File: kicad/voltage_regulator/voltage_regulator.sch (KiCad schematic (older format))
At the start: 14 parts

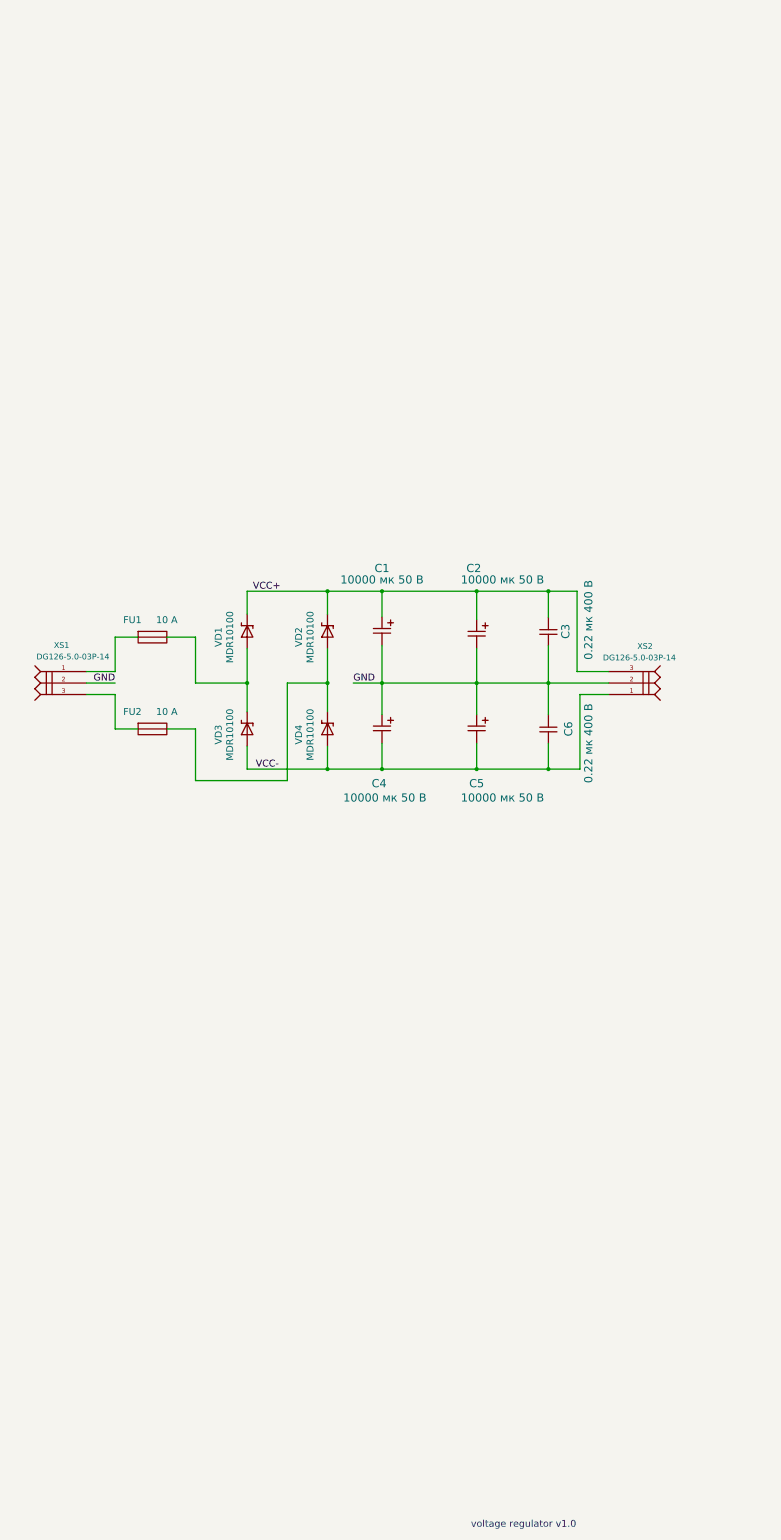
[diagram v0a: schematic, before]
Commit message: Add emc filter.
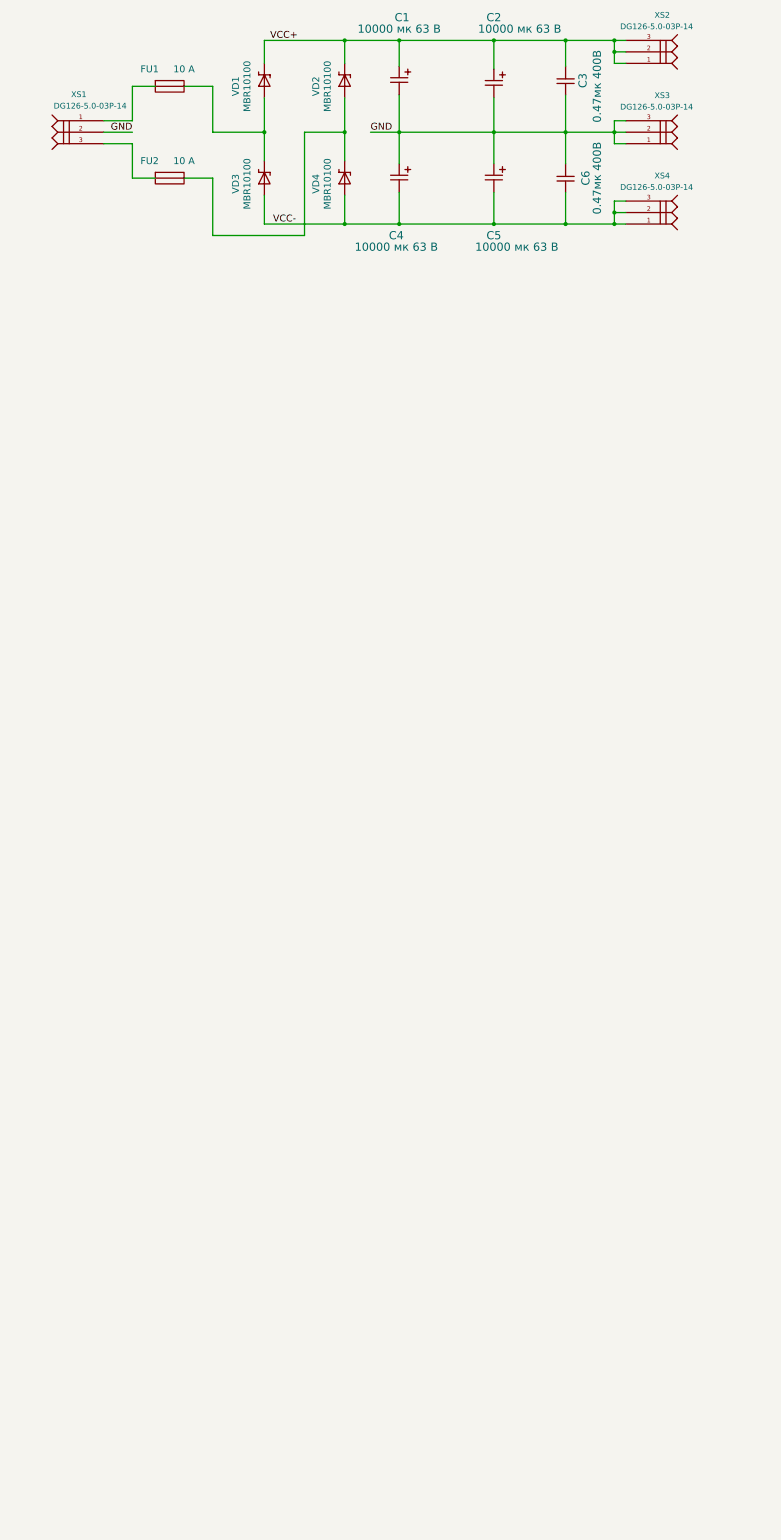
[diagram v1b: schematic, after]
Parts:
- added XS2, XS4: DG126-5.0-03P-14, ~, symbol PIN_F_3
- C1, C2, C4, C5: value 10000 мк 50 В -> 10000 мк 63 В
- C3, C6: value 0.22 мк 400 В -> 0.47мк 400В
- VD1, VD2, VD3, VD4: value MDR10100 -> MBR10100
- renumbered XS2 to XS3
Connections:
- net GND: now also XS3.1, XS3.3
- net VCC+: now also XS2.1, XS2.2, XS2.3; no longer XS3.3
- net VCC-: now also XS4.1, XS4.2, XS4.3; no longer XS3.1
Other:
- note removed: "voltage regulator v1.0"
- moved on the sheet: C1, C2, C3, C4, C5, C6, FU1, FU2, VD1, VD2, VD3, VD4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

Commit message: Moved to kicad 4.0.0
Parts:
- C1, C2, C4, C5: footprint (none) -> LFcomponents:CAPACITOR_CD294
- C3, C6: footprint (none) -> LFcomponents:K73-17
- FU1, FU2: footprint (none) -> LFcomponents:FU_PTF15B
- VD1, VD2, VD3, VD4: footprint (none) -> LFcomponents:TO220_DIOD_VERT_POZ
- XS1, XS2, XS3, XS4: footprint ~ -> DG126-5.0-03P-14~
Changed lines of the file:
@@
 LIBS:LFtransistor
 LIBS:voltage_regulator-cache
-EELAYER 27 0
+EELAYER 25 0
 EELAYER END
 $Descr A4 11693 8268
@@
 F 0 "C5" V 7475 4375 71  0000 C CNN
 F 1 "10000 мк 63 В" V 7575 4575 71  0000 C CNN
-F 2 "" H 6850 4375 60  0001 C CNN
+F 2 "LFcomponents:CAPACITOR_CD294" H 6850 4375 60  0001 C CNN
 F 3 "" H 6850 4375 60  0001 C CNN
 	1    6850 4375
@@
 F 0 "C2" V 6400 3550 71  0000 C CNN
 F 1 "10000 мк 63 В" V 6500 3775 71  0000 C CNN
-F 2 "" H 6850 3550 60  0001 C CNN
+F 2 "LFcomponents:CAPACITOR_CD294" H 6850 3550 60  0001 C CNN
 F 3 "" H 6850 3550 60  0001 C CNN
 	1    6850 3550
@@
 F 0 "C6" H 7600 4450 71  0000 C CNN
 F 1 "0.47мк 400В" H 7600 4350 71  0000 C CNN
-F 2 "" H 7475 4625 60  0001 C CNN
+F 2 "LFcomponents:K73-17" H 7475 4625 60  0001 C CNN
 F 3 "" H 7475 4625 60  0001 C CNN
 	1    7475 4625
@@
 F 0 "C4" V 6650 4350 71  0000 C CNN
 F 1 "10000 мк 63 В" V 6750 4350 71  0000 C CNN
-F 2 "" H 6025 4375 60  0001 C CNN
+F 2 "LFcomponents:CAPACITOR_CD294" H 6025 4375 60  0001 C CNN
 F 3 "" H 6025 4375 60  0001 C CNN
 	1    6025 4375
@@
 F 0 "C1" V 5600 3550 71  0000 C CNN
 F 1 "10000 мк 63 В" V 5700 3525 71  0000 C CNN
-F 2 "" H 6025 3525 60  0001 C CNN
+F 2 "LFcomponents:CAPACITOR_CD294" H 6025 3525 60  0001 C CNN
 F 3 "" H 6025 3525 60  0001 C CNN
 	1    6025 3525
@@
 F 0 "C3" H 7600 3625 71  0000 C CNN
 F 1 "0.47мк 400В" H 7550 3500 71  0000 C CNN
-F 2 "" H 7475 3775 60  0001 C CNN
+F 2 "LFcomponents:K73-17" H 7475 3775 60  0001 C CNN
 F 3 "" H 7475 3775 60  0001 C CNN
 	1    7475 3775
@@
 F 0 "XS3" H 8250 3750 50  0000 L BNN
 F 1 "DG126-5.0-03P-14" H 7950 3850 50  0000 L BNN
-F 2 "~" H 8450 4350 50  0001 C CNN
+F 2 "DG126-5.0-03P-14~" H 8450 4350 50  0001 C CNN
 F 3 "" H 8000 4200 60  0001 C CNN
 	1    8000 4200
@@
 F 0 "FU2" H 3850 4650 60  0000 C CNN
 F 1 "10 A" H 4150 4650 60  0000 C CNN
-F 2 "" H 3900 4500 60  0001 C CNN
+F 2 "LFcomponents:FU_PTF15B" H 3900 4500 60  0001 C CNN
 F 3 "" H 3900 4500 60  0001 C CNN
 	1    3900 4500
@@
 F 0 "VD4" H 5650 4900 60  0000 C CNN
 F 1 "MBR10100" H 5650 4800 60  0000 C CNN
-F 2 "" H 5550 4650 60  0001 C CNN
+F 2 "LFcomponents:TO220_DIOD_VERT_POZ" H 5550 4650 60  0001 C CNN
 F 3 "" H 5550 4650 60  0001 C CNN
 	1    5550 4650
@@
 F 0 "VD3" H 4950 4900 60  0000 C CNN
 F 1 "MBR10100" H 4950 4800 60  0000 C CNN
-F 2 "" H 4850 4650 60  0001 C CNN
+F 2 "LFcomponents:TO220_DIOD_VERT_POZ" H 4850 4650 60  0001 C CNN
 F 3 "" H 4850 4650 60  0001 C CNN
 	1    4850 4650
@@
 F 0 "VD2" H 5650 4050 60  0000 C CNN
 F 1 "MBR10100" H 5650 3950 60  0000 C CNN
-F 2 "" H 5550 3800 60  0001 C CNN
+F 2 "LFcomponents:TO220_DIOD_VERT_POZ" H 5550 3800 60  0001 C CNN
 F 3 "" H 5550 3800 60  0001 C CNN
 	1    5550 3800
@@
 F 0 "FU1" H 3850 3850 60  0000 C CNN
 F 1 "10 A" H 4150 3850 60  0000 C CNN
-F 2 "" H 3900 3700 60  0001 C CNN
+F 2 "LFcomponents:FU_PTF15B" H 3900 3700 60  0001 C CNN
 F 3 "" H 3900 3700 60  0001 C CNN
 	1    3900 3700
@@
 F 0 "XS1" H 3600 4200 50  0000 L BNN
 F 1 "DG126-5.0-03P-14" H 3250 4100 50  0000 L BNN
-F 2 "~" H 3900 4150 50  0001 C CNN
+F 2 "DG126-5.0-03P-14~" H 3900 4150 50  0001 C CNN
 F 3 "" H 3450 4000 60  0001 C CNN
 	1    3450 4000
@@
 F 0 "VD1" H 4950 4050 60  0000 C CNN
 F 1 "MBR10100" H 4950 3950 60  0000 C CNN
-F 2 "" H 4850 3800 60  0001 C CNN
+F 2 "LFcomponents:TO220_DIOD_VERT_POZ" H 4850 3800 60  0001 C CNN
 F 3 "" H 4850 3800 60  0001 C CNN
 	1    4850 3800
@@
 F 0 "XS2" H 8250 3050 50  0000 L BNN
 F 1 "DG126-5.0-03P-14" H 7950 3150 50  0000 L BNN
-F 2 "~" H 8450 3650 50  0001 C CNN
+F 2 "DG126-5.0-03P-14~" H 8450 3650 50  0001 C CNN
 F 3 "" H 8000 3500 60  0001 C CNN
 	1    8000 3500
@@
 F 0 "XS4" H 8250 4450 50  0000 L BNN
 F 1 "DG126-5.0-03P-14" H 7950 4550 50  0000 L BNN
-F 2 "~" H 8450 5050 50  0001 C CNN
+F 2 "DG126-5.0-03P-14~" H 8450 5050 50  0001 C CNN
 F 3 "" H 8000 4900 60  0001 C CNN
 	1    8000 4900

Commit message: Add description to the schemes.
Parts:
- added R1, R2: 20 к, LFcomponents:RESISTOR_1W, symbol RESISTOR_1W
- C1, C2, C4, C5: value 10000 мк 63 В -> 10000 мк 50 В
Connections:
- net GND: now also R1.2, R2.1
- net VCC+: now also R1.1
- net VCC-: now also R2.2
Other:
- moved on the sheet: XS2, XS3, XS4
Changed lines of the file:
@@
 	6850 3300 6850 3550
 Wire Wire Line
-	5775 4100 8000 4100
+	5775 4100 8450 4100
 Connection ~ 7475 3300
 Connection ~ 5550 3300
@@
 Connection ~ 6025 4100
 Wire Wire Line
-	4850 4900 8000 4900
+	4850 4900 8450 4900
 Connection ~ 7475 4900
 Wire Wire Line
@@
 P 6850 4375
 F 0 "C5" V 7475 4375 71  0000 C CNN
-F 1 "10000 мк 63 В" V 7575 4575 71  0000 C CNN
+F 1 "10000 мк 50 В" V 7575 4575 71  0000 C CNN
 F 2 "LFcomponents:CAPACITOR_CD294" H 6850 4375 60  0001 C CNN
 F 3 "" H 6850 4375 60  0001 C CNN
@@
 P 6850 3550
 F 0 "C2" V 6400 3550 71  0000 C CNN
-F 1 "10000 мк 63 В" V 6500 3775 71  0000 C CNN
+F 1 "10000 мк 50 В" V 6500 3775 71  0000 C CNN
 F 2 "LFcomponents:CAPACITOR_CD294" H 6850 3550 60  0001 C CNN
 F 3 "" H 6850 3550 60  0001 C CNN
@@
 P 6025 4375
 F 0 "C4" V 6650 4350 71  0000 C CNN
-F 1 "10000 мк 63 В" V 6750 4350 71  0000 C CNN
+F 1 "10000 мк 50 В" V 6750 4350 71  0000 C CNN
 F 2 "LFcomponents:CAPACITOR_CD294" H 6025 4375 60  0001 C CNN
 F 3 "" H 6025 4375 60  0001 C CNN
@@
 P 6025 3525
 F 0 "C1" V 5600 3550 71  0000 C CNN
-F 1 "10000 мк 63 В" V 5700 3525 71  0000 C CNN
+F 1 "10000 мк 50 В" V 5700 3525 71  0000 C CNN
 F 2 "LFcomponents:CAPACITOR_CD294" H 6025 3525 60  0001 C CNN
 F 3 "" H 6025 3525 60  0001 C CNN
@@
 L PIN_F_3 XS?
 U 1 1 51AC3EE1
-P 8000 4200
+P 8450 4200
 AR Path="/51AC3C4F" Ref="XS?"  Part="1"
 AR Path="/51AC3EE1" Ref="XS3"  Part="1"
-F 0 "XS3" H 8250 3750 50  0000 L BNN
-F 1 "DG126-5.0-03P-14" H 7950 3850 50  0000 L BNN
-F 2 "DG126-5.0-03P-14~" H 8450 4350 50  0001 C CNN
-F 3 "" H 8000 4200 60  0001 C CNN
-	1    8000 4200
+F 0 "XS3" H 8700 3750 50  0000 L BNN
+F 1 "DG126-5.0-03P-14" H 8400 3850 50  0000 L BNN
+F 2 "DG126-5.0-03P-14~" H 8900 4350 50  0001 C CNN
+F 3 "" H 8450 4200 60  0001 C CNN
+	1    8450 4200
 	1    0    0    1
 $EndComp
@@
 L PIN_F_3 XS?
 U 1 1 55744C00
-P 8000 3500
+P 8450 3500
 AR Path="/51AC3C4F" Ref="XS?"  Part="1"
 AR Path="/55744C00" Ref="XS2"  Part="1"
-F 0 "XS2" H 8250 3050 50  0000 L BNN
-F 1 "DG126-5.0-03P-14" H 7950 3150 50  0000 L BNN
-F 2 "DG126-5.0-03P-14~" H 8450 3650 50  0001 C CNN
-F 3 "" H 8000 3500 60  0001 C CNN
-	1    8000 3500
+F 0 "XS2" H 8700 3050 50  0000 L BNN
+F 1 "DG126-5.0-03P-14" H 8400 3150 50  0000 L BNN
+F 2 "DG126-5.0-03P-14~" H 8900 3650 50  0001 C CNN
+F 3 "" H 8450 3500 60  0001 C CNN
+	1    8450 3500
 	1    0    0    1
 $EndComp
@@
 L PIN_F_3 XS?
 U 1 1 55744C06
-P 8000 4900
+P 8450 4900
 AR Path="/51AC3C4F" Ref="XS?"  Part="1"
 AR Path="/55744C06" Ref="XS4"  Part="1"
-F 0 "XS4" H 8250 4450 50  0000 L BNN
-F 1 "DG126-5.0-03P-14" H 7950 4550 50  0000 L BNN
-F 2 "DG126-5.0-03P-14~" H 8450 5050 50  0001 C CNN
-F 3 "" H 8000 4900 60  0001 C CNN
-	1    8000 4900
+F 0 "XS4" H 8700 4450 50  0000 L BNN
+F 1 "DG126-5.0-03P-14" H 8400 4550 50  0000 L BNN
+F 2 "DG126-5.0-03P-14~" H 8900 5050 50  0001 C CNN
+F 3 "" H 8450 4900 60  0001 C CNN
+	1    8450 4900
 	1    0    0    1
 $EndComp
 Wire Wire Line
-	4850 3300 8000 3300
-Wire Wire Line
-	8000 3400 7900 3400
-Wire Wire Line
-	7900 3300 7900 3500
-Connection ~ 7900 3300
-Wire Wire Line
-	7900 3500 8000 3500
-Connection ~ 7900 3400
-Wire Wire Line
-	7900 4700 7900 4900
-Wire Wire Line
-	7900 4700 8000 4700
-Connection ~ 7900 4900
-Wire Wire Line
-	8000 4800 7900 4800
-Connection ~ 7900 4800
-Wire Wire Line
-	7900 4200 8000 4200
-Wire Wire Line
-	7900 4000 7900 4200
-Connection ~ 7900 4100
-Wire Wire Line
-	7900 4000 8000 4000
+	4850 3300 8450 3300
+Wire Wire Line
+	8450 3400 8350 3400
+Wire Wire Line
+	8350 3300 8350 3500
+Connection ~ 8350 3300
+Wire Wire Line
+	8350 3500 8450 3500
+Connection ~ 8350 3400
+Wire Wire Line
+	8350 4700 8350 4900
+Wire Wire Line
+	8350 4700 8450 4700
+Connection ~ 8350 4900
+Wire Wire Line
+	8450 4800 8350 4800
+Connection ~ 8350 4800
+Wire Wire Line
+	8350 4200 8450 4200
+Wire Wire Line
+	8350 4000 8350 4200
+Connection ~ 8350 4100
+Wire Wire Line
+	8350 4000 8450 4000
+$Comp
+L RESISTOR_1W R1
+U 1 1 56962990
+P 8050 3550
+F 0 "R1" H 8350 3700 71  0000 C CNN
+F 1 "20 к" H 8050 3700 71  0000 C CNN
+F 2 "LFcomponents:RESISTOR_1W" H 8050 3550 60  0001 C CNN
+F 3 "" H 8050 3550 60  0000 C CNN
+	1    8050 3550
+	0    1    1    0
+$EndComp
+$Comp
+L RESISTOR_1W R2
+U 1 1 56962C17
+P 8050 4400
+F 0 "R2" H 8350 4550 71  0000 C CNN
+F 1 "20 к" H 8050 4550 71  0000 C CNN
+F 2 "LFcomponents:RESISTOR_1W" H 8050 4400 60  0001 C CNN
+F 3 "" H 8050 4400 60  0000 C CNN
+	1    8050 4400
+	0    1    1    0
+$EndComp
+Wire Wire Line
+	8050 3800 8050 4400
+Connection ~ 8050 4100
+Wire Wire Line
+	8050 3550 8050 3300
+Connection ~ 8050 3300
+Wire Wire Line
+	8050 4650 8050 4900
+Connection ~ 8050 4900
 $EndSCHEMATC
